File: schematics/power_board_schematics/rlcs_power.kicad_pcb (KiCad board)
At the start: 2 copper layers, 57.2 x 105.4 mm, 55 parts, among them J1 Conn_01x05_Male, J2 Conn_01x05_Male, J3 SD_Card, J4 Battery Conn, J5 Battery Conn, J6 CONN_01X02, J7 CONN_01X02, J8 CONN_01X02, Q1 Q_NPN_BEC, Q2 Q_NPN_BEC, T1 12 to 3v3, T2 12 to 5

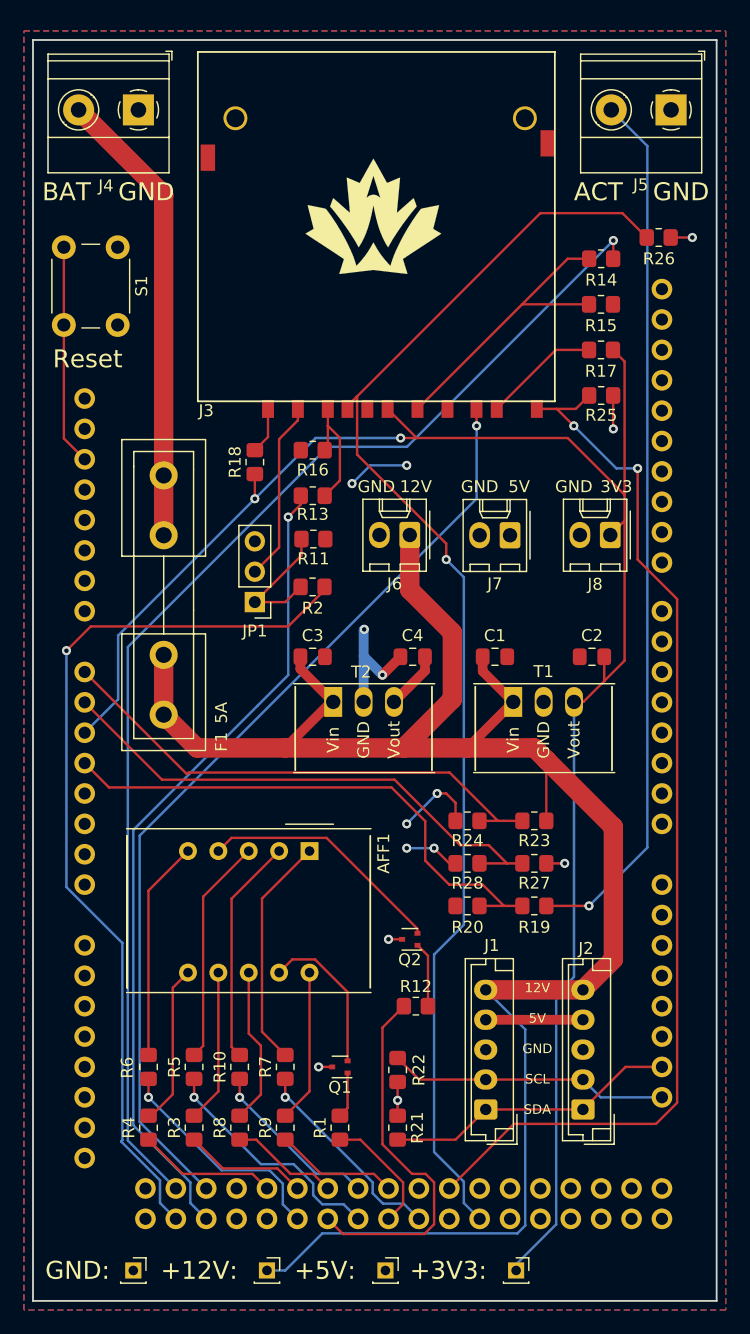
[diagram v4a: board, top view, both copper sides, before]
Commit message: Update Towerside Power Board PCB layout
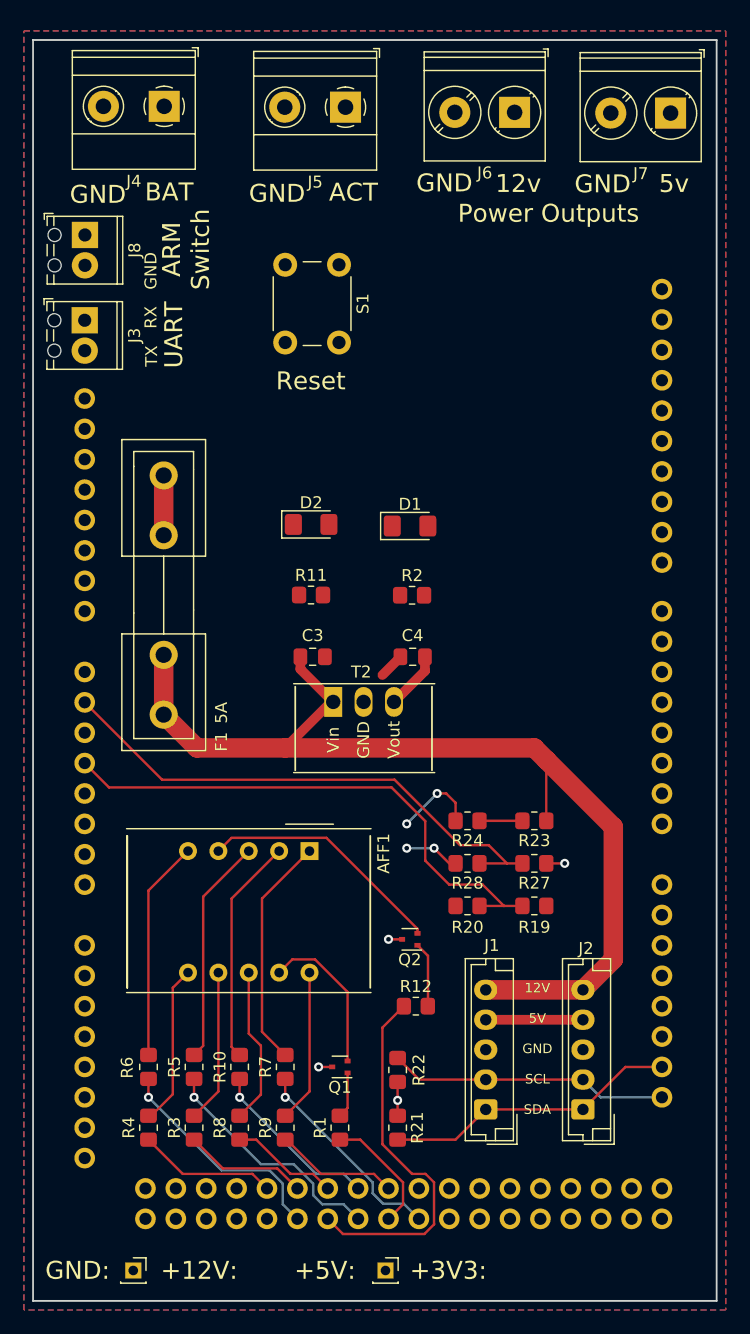
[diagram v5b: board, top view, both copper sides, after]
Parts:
- removed C1: 10uF, Capacitor_SMD:C_0805_2012Metric_Pad1.15x1.40mm_HandSolder
- removed C2: 22uF, Capacitor_SMD:C_0805_2012Metric_Pad1.15x1.40mm_HandSolder
- removed G*** (x2): LOGO, rlcs_power_footprints:rocketry_logo_small_noletters
- removed JP1: Jumper_NC_Dual, Connector_PinHeader_2.54mm:PinHeader_1x03_P2.54mm_Vertical
- removed R13, R14, R25, R26: 10K, Resistor_SMD:R_0805_2012Metric_Pad1.20x1.40mm_HandSolder
- removed R15, R16, R17, R18: 20K, Resistor_SMD:R_0805_2012Metric_Pad1.20x1.40mm_HandSolder
- removed T1: 12 to 3v3, rlcs_power_footprints:VXO78XX-1000
- removed TP1: 12v_test, Connector_PinSocket_2.00mm:PinSocket_1x01_P2.00mm_Vertical
- removed TP2: 3v3_test, Connector_PinSocket_2.00mm:PinSocket_1x01_P2.00mm_Vertical
- added D1: Green, LED_SMD:LED_1206_3216Metric_Pad1.42x1.75mm_HandSolder, F.Cu at (124.2, 102.9)
- added D2: Red, LED_SMD:LED_1206_3216Metric_Pad1.42x1.75mm_HandSolder, F.Cu at (116.0, 102.7)
- F1: value Fuse_Small -> 5A
- J3: value SD_Card -> UART Conn; footprint rlcs_power_footprints:SDCARD -> TerminalBlock_Phoenix:TerminalBlock_Phoenix_MPT-0,5-2-2.54_1x02_P2.54mm_Horizontal
- J4: value Battery Conn -> Power Board Power Input; footprint TerminalBlock_Phoenix:TerminalBlock_Phoenix_MKDS-1,5-2_1x02_P5.00mm_Horizontal -> TerminalBlock_Phoenix:TerminalBlock_Phoenix_MKDS-1,5-2-5.08_1x02_P5.08mm_Horizontal
- J5: value Battery Conn -> Actuator Battery Conn; footprint TerminalBlock_Phoenix:TerminalBlock_Phoenix_MKDS-1,5-2_1x02_P5.00mm_Horizontal -> TerminalBlock_Phoenix:TerminalBlock_Phoenix_MKDS-1,5-2-5.08_1x02_P5.08mm_Horizontal
- J6: value CONN_01X02 -> 12v Output; footprint Connector_Molex:Molex_KK-254_AE-6410-02A_1x02_P2.54mm_Vertical -> TerminalBlock_Phoenix:TerminalBlock_Phoenix_PT-1,5-2-5.0-H_1x02_P5.00mm_Horizontal
- J7: value CONN_01X02 -> 5v Output; footprint Connector_Molex:Molex_KK-254_AE-6410-02A_1x02_P2.54mm_Vertical -> TerminalBlock_Phoenix:TerminalBlock_Phoenix_PT-1,5-2-5.0-H_1x02_P5.00mm_Horizontal
- J8: value CONN_01X02 -> Keylock Switch Conn; footprint Connector_Molex:Molex_KK-254_AE-6410-02A_1x02_P2.54mm_Vertical -> TerminalBlock_Phoenix:TerminalBlock_Phoenix_MPT-0,5-2-2.54_1x02_P2.54mm_Horizontal
- R11: value 10K -> 150
- R2: value 20K -> 150
- moved J8 50.6 mm to (97.0, 78.5), turned to -90 degrees
- moved J7 37.8 mm to (146.0, 68.3)
- moved J6 36.4 mm to (133.0, 68.3)
- moved J5 27.2 mm to (118.8, 67.8)
- moved J3 25.8 mm to (97.0, 85.7), turned to -90 degrees
- moved S1 18.6 mm to (118.3, 81.0)
- moved R2 8.35 mm to (124.4, 108.7)
- moved R11 4.68 mm to (116.0, 108.6), turned to 0 degrees
- moved J4 2.18 mm to (103.7, 67.8)
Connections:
- J3 pad 1: Net-(J3-Pad1) -> ARD_UART_TX
- J3 pad 2: Net-(J3-Pad2) -> ARD_UART_RX
- J4 pad 1: GND -> Net-(F1-Pad1)
- J4 pad 2: Net-(F1-Pad1) -> GND
- J5 pad 1: GND -> /ACTUATOR_BAT
- J5 pad 2: /ACTUATOR_BAT -> GND
- J8 pad 1: SENSE_3V -> ARD_ARM_SWITCH
- R1 pad 1: Sevenseg_D2 -> Sevenseg_D1
- R11 pad 1: GND -> ARD_LED_ARMED
- R11 pad 2: Net-(JP1-Pad1) -> Net-(D2-Pad2)
- R12 pad 1: Sevenseg_D1 -> Sevenseg_D2
- R2 pad 1: Net-(JP1-Pad1) -> ARD_LED_CLIENT_COMM
- R2 pad 2: ARD_CON_SD_SS -> Net-(D1-Pad2)
- XA1 pad A0: SENSE_12V -> unconnected-(XA1-PadA0)
- XA1 pad A2: SENSE_3V -> unconnected-(XA1-PadA2)
- XA1 pad A4: unconnected-(XA1-PadA4) -> SENSE_12V
- XA1 pad D0: unconnected-(XA1-PadD0) -> ARD_UART_RX
- XA1 pad D1: unconnected-(XA1-PadD1) -> ARD_UART_TX
- XA1 pad D33: ARD_CON_SD_CD -> unconnected-(XA1-PadD33)
- XA1 pad D34: ARD_CON_SD_WP -> ARD_ARM_SWITCH
- XA1 pad D35: unconnected-(XA1-PadD35) -> ARD_LED_CLIENT_COMM
- XA1 pad D36: unconnected-(XA1-PadD36) -> ARD_LED_ARMED
- XA1 pad D39: Sevenseg_D2 -> Sevenseg_D1
- XA1 pad D43: Sevenseg_D1 -> Sevenseg_D2
- XA1 pad D50: ARD_CON_SD_MISO -> unconnected-(XA1-PadD50)
- XA1 pad D51: ARD_CON_SD_MOSI -> unconnected-(XA1-PadD51)
- XA1 pad D52: ARD_CON_SD_SCK -> unconnected-(XA1-PadD52)
- XA1 pad D53: ARD_CON_SD_SS -> unconnected-(XA1-PadD53)
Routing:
- net SENSE_3V: track 151.2 -> 0.00 mm, vias 2 -> 0
- net ARD_CON_SD_CD: track 107.8 -> 0.00 mm, vias 1 -> 0
- net ARD_CON_SD_SCK: track 103.1 -> 0.00 mm, vias 1 -> 0
- net ARD_CON_SD_WP: track 90.1 -> 0.00 mm, vias 2 -> 0
- net ARD_CON_SD_MISO: track 79.1 -> 0.00 mm, vias 1 -> 0
- net +12V: track 160.3 -> 84.9 mm
- net ARD_CON_SD_SS: track 75.3 -> 0.00 mm, vias 1 -> 0
- net /ACTUATOR_BAT: track 73.4 -> 0.00 mm, vias 1 -> 0
- net ARD_CON_SD_MOSI: track 68.8 -> 0.00 mm, vias 1 -> 0
- net SENSE_12V: track 43.4 -> 3.59 mm
- net Net-(F1-Pad1): track 38.5 -> 5.00 mm
- net Net-(J3-Pad5): track 25.1 -> 0.00 mm
- net Sevenseg_D2: track 10.3 -> 31.2 mm
- net Sevenseg_D1: track 31.2 -> 10.3 mm
- net Net-(S1-Pad2): track 18.4 -> 0.00 mm
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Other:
- board text added: "12v"
- board text added: "5v"
- board text added: "ARM Switch"
- board text added: "Power Outputs"
- board text added: "RX"
- board text added: "TX"
- board text added: "UART"

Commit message: Layout Towerside Power Board
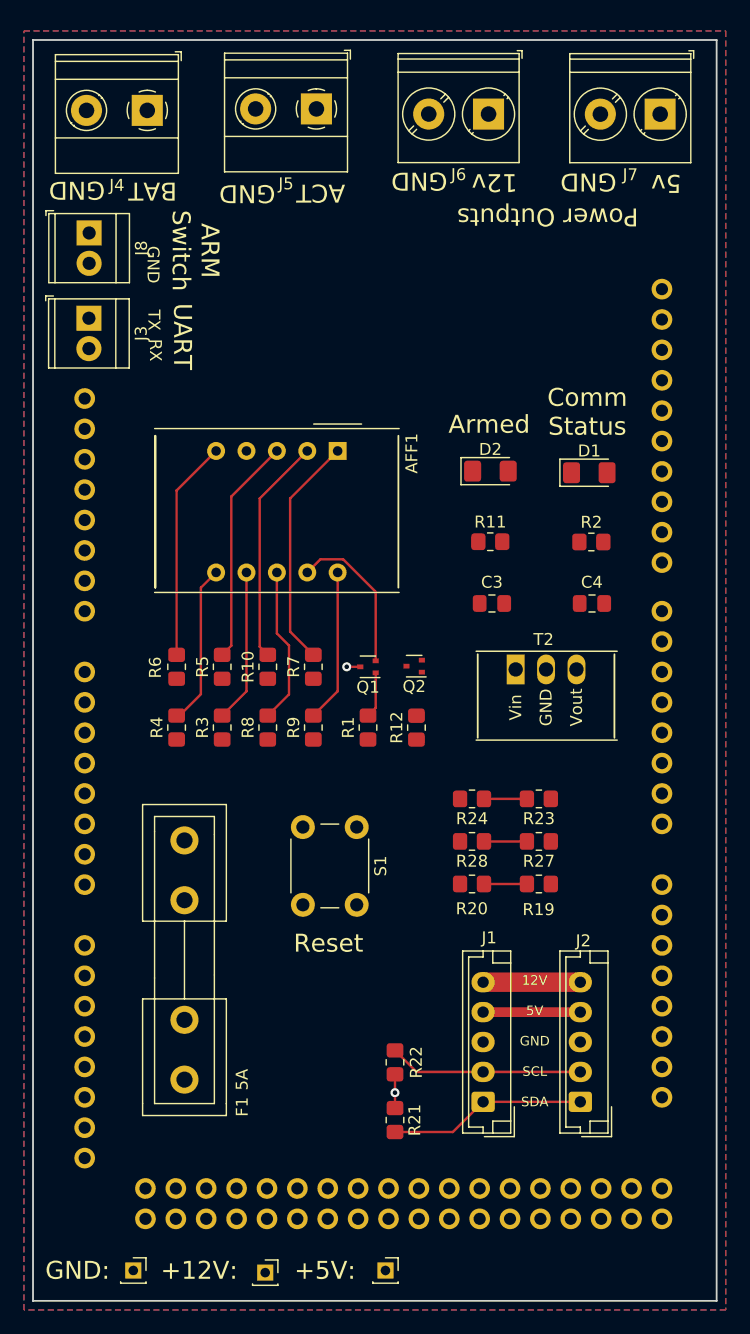
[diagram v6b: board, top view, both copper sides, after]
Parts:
- added TP1: 12v_test, Connector_PinSocket_2.00mm:PinSocket_1x01_P2.00mm_Vertical, F.Cu at (112.1, 165.3)
- J3, J8: footprint TerminalBlock_Phoenix:TerminalBlock_Phoenix_MPT-0,5-2-2.54_1x02_P2.54mm_Horizontal -> TerminalBlock_TE-Connectivity:TerminalBlock_TE_282834-2_1x02_P2.54mm_Horizontal
- moved S1 47.0 mm to (119.8, 128.0)
- moved R1 33.5 mm to (120.7, 119.7)
- moved R3 33.5 mm to (108.5, 119.7)
- moved R4 33.5 mm to (104.7, 119.7)
- moved R8 33.5 mm to (112.3, 119.7)
- moved R9 33.5 mm to (116.1, 119.7)
- moved AFF1 33.5 mm to (118.2, 96.6)
- moved Q1 33.5 mm to (120.7, 114.6)
- moved R10 33.5 mm to (112.3, 114.6)
- moved R5 33.5 mm to (108.5, 114.6)
- moved R6 33.5 mm to (104.7, 114.6)
- moved R7 33.5 mm to (116.1, 114.6)
- moved F1 30.6 mm to (105.4, 129.1)
- moved R12 23.3 mm to (124.8, 119.7), turned to 90 degrees
- moved Q2 22.8 mm to (124.6, 114.6)
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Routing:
- net +12V: track 84.9 -> 8.13 mm
- net SENSE_ACTUATOR: track 45.5 -> 3.59 mm
- net SENSE_5V: track 44.5 -> 3.59 mm
- net Sevenseg_D2: track 31.2 -> 0.00 mm
- net Net-(AFF1-Pad4): track 20.6 -> 0.00 mm
- net Sevenseg_E: track 20.0 -> 0.00 mm, vias 1 -> 0
- net Sevenseg_D: track 19.2 -> 0.00 mm, vias 1 -> 0
- net Sevenseg_C: track 17.5 -> 0.00 mm, vias 1 -> 0
- net Sevenseg_DP: track 14.6 -> 0.00 mm, vias 1 -> 0
- net GND: track 13.7 -> 0.00 mm, vias 4 -> 0
- net Sevenseg_F: track 11.6 -> 0.00 mm
- net Sevenseg_G: track 10.3 -> 0.00 mm
- net Sevenseg_A: track 10.3 -> 0.00 mm
- net Sevenseg_D1: track 10.3 -> 0.00 mm
- net Sevenseg_B: track 9.06 -> 0.00 mm
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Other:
- board text added: "Armed"
- board text added: "Comm Status"
- board text added: "RLCSv3 Power Board {dblquote}The Juice{dblquote} R4 2022-11-02 Jack Christensen Jason Xu"
- board text removed: "+3V3:"
- board text removed: "RLCSv3 Power Board {dblquote}The Juice{dblquote} R3 2022-01-27 Jack Christensen"

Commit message: Update Towerside Power Board silkscreen
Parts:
- moved S1 2.48 mm to (120.1, 130.5)
- moved TP4 2.02 mm to (124.2, 165.3)
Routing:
- net +12V: track 8.13 -> 0.00 mm
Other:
- board text added: "Current State"
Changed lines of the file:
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@@
       (effects (font (size 0.8 0.8) (thickness 0.15)))
     )
-    (fp_text user "GND" (at 5.08 4.318) (layer "F.SilkS")
+    (fp_text user "GND" (at 5.08 4.318 180) (layer "F.SilkS")
       (effects (font (size 0.8 0.8) (thickness 0.15)))
     )
-    (fp_text user "5V" (at 7.62 4.318) (layer "F.SilkS")
+    (fp_text user "5V" (at 7.62 4.318 180) (layer "F.SilkS")
       (effects (font (size 0.8 0.8) (thickness 0.15)))
     )
-    (fp_text user "SDA" (at 0 4.318) (layer "F.SilkS")
+    (fp_text user "SDA" (at 0 4.318 180) (layer "F.SilkS")
       (effects (font (size 0.8 0.8) (thickness 0.15)))
     )
@@
   )
   (footprint "Connector_PinSocket_2.00mm:PinSocket_1x01_P2.00mm_Vertical" (layer "F.Cu")
-    (at 122.174 165.1)
+    (at 124.19 165.28)
     (descr "Through hole straight socket strip, 1x01, 2.00mm pitch, single row (from Kicad 4.0.7), script generated")
     (tags "Through hole socket strip THT 1x01 2.00mm single row")
@@
   )
   (footprint "Button_Switch_THT:SW_PUSH_6mm" (layer "F.Cu")
-    (at 119.77 128.03 -90)
+    (at 120.08 130.49 -90)
     (descr "https://www.omron.com/ecb/products/pdf/en-b3f.pdf")
     (tags "tact sw push 6mm")
@@
     (effects (font (size 1.2 1.2) (thickness 0.15)) (justify left mirror))
   )
-  (gr_text "Armed" (at 130.85 94.37) (layer "F.SilkS")
+  (gr_text "Armed" (at 130.85 94.37 180) (layer "F.SilkS")
     (effects (font (size 1.5 1.5) (thickness 0.3)))
   )
-  (gr_text "RX" (at 102.95 88.16 -90) (layer "F.SilkS")
+  (gr_text "RX" (at 103.22 88.15 -90) (layer "F.SilkS")
     (effects (font (size 1 1) (thickness 0.15)))
   )
@@
     (effects (font (size 1.5 1.5) (thickness 0.3)) (justify left))
   )
-  (gr_text "TX" (at 102.82 85.65 -90) (layer "F.SilkS")
+  (gr_text "TX" (at 103.26 85.6 -90) (layer "F.SilkS")
     (effects (font (size 1 1) (thickness 0.15)))
   )
@@
     (effects (font (size 1.5 1.5) (thickness 0.3)) (justify left))
   )
-  (gr_text "UART" (at 105.2 87.02 -90) (layer "F.SilkS")
+  (gr_text "Current State" (at 113.09 92.56 180) (layer "F.SilkS")
+    (effects (font (size 1.5 1.5) (thickness 0.3)))
+  )
+  (gr_text "UART" (at 105.39 87.27 -90) (layer "F.SilkS")
     (effects (font (size 1.5 1.5) (thickness 0.3)))
   )
@@
     (effects (font (size 1.5 1.5) (thickness 0.3)) (justify left))
   )
-  (gr_text "+5V:" (at 114.554 165.1) (layer "F.SilkS")
+  (gr_text "+5V:" (at 131.36 165.28 180) (layer "F.SilkS")
     (effects (font (size 1.5 1.5) (thickness 0.3)) (justify left))
   )
-  (gr_text "GND" (at 102.75 81.01 -90) (layer "F.SilkS")
+  (gr_text "GND" (at 103.37 80.96 -90) (layer "F.SilkS")
     (effects (font (size 1 1) (thickness 0.15)))
   )
-  (gr_text "+12V:" (at 103.378 165.1) (layer "F.SilkS")
+  (gr_text "+12V:" (at 120.75 165.3 180) (layer "F.SilkS")
     (effects (font (size 1.5 1.5) (thickness 0.3)) (justify left))
   )
-  (gr_text "GND:\n" (at 93.726 165.1) (layer "F.SilkS")
+  (gr_text "GND:\n" (at 108.16 165.2 180) (layer "F.SilkS")
     (effects (font (size 1.5 1.5) (thickness 0.3)) (justify left))
   )
-  (gr_text "ARM\nSwitch" (at 106.29 79.84 -90) (layer "F.SilkS")
+  (gr_text "ARM\nSwitch" (at 106.75 79.85 -90) (layer "F.SilkS")
     (effects (font (size 1.5 1.5) (thickness 0.3)))
   )
@@
     (effects (font (size 1.5 1.5) (thickness 0.3)) (justify left))
   )
-  (gr_text "12v" (at 133.22 74.14 180) (layer "F.SilkS")
+  (gr_text "12v" (at 133.33 74.08 180) (layer "F.SilkS")
     (effects (font (size 1.5 1.5) (thickness 0.3)) (justify left))
   )
-  (gr_text "Comm\nStatus" (at 139.05 93.33) (layer "F.SilkS")
+  (gr_text "Comm\nStatus" (at 139.05 93.33 180) (layer "F.SilkS")
     (effects (font (size 1.5 1.5) (thickness 0.3)))
   )
-  (gr_text "Reset" (at 117.41 137.75) (layer "F.SilkS")
+  (gr_text "Reset" (at 117.78 127.51 180) (layer "F.SilkS")
     (effects (font (size 1.5 1.5) (thickness 0.3)))
   )
@@
   (segment (start 116.74 105.64) (end 118.632642 105.64) (width 0.2032) (layer "F.Cu") (net 22))
   (segment (start 115.634889 106.745111) (end 116.74 105.64) (width 0.2032) (layer "F.Cu") (net 22))
-  (segment (start 138.464 141) (end 130.336 141) (width 1.6256) (layer "F.Cu") (net 26))
   (segment (start 130.41 125.674) (end 133.998 125.674) (width 0.2032) (layer "F.Cu") (net 38))
   (segment (start 130.41 129.23) (end 133.998 129.23) (width 0.2032) (layer "F.Cu") (net 39))

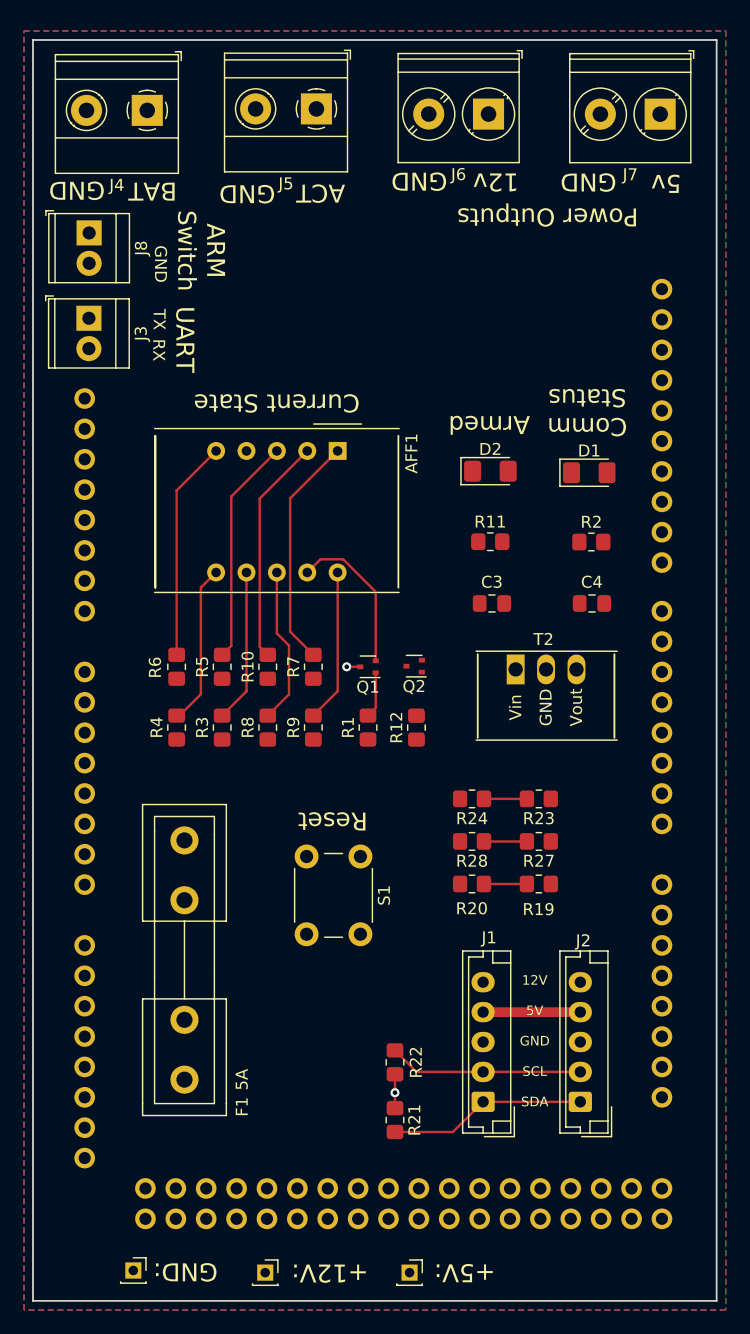
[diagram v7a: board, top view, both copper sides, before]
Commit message: Route Towerside Power Board
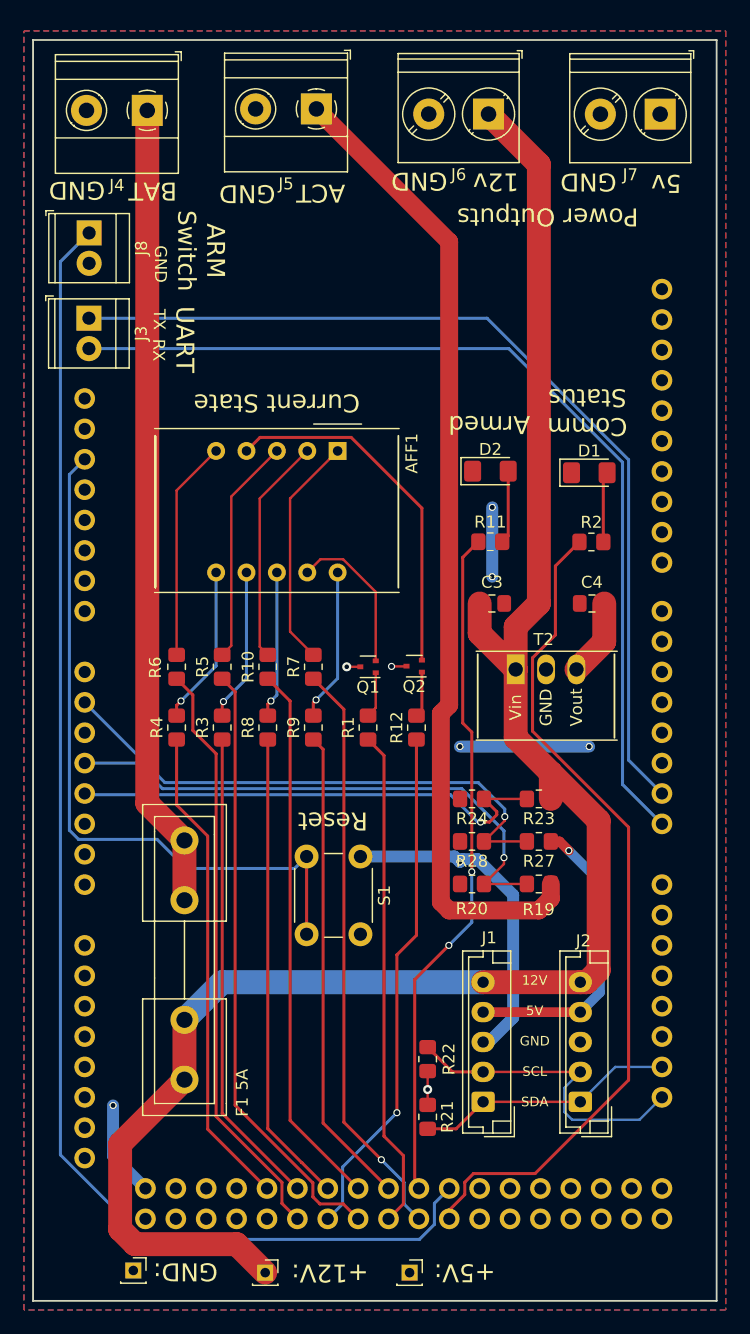
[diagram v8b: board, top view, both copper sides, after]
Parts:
- moved R21 2.74 mm to (125.7, 152.3)
- moved R22 2.74 mm to (125.7, 147.4)
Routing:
- net +12V: track 0.00 -> 155.7 mm
- net ARD_ARM_SWITCH: track 0.00 -> 116.3 mm
- net /ACTUATOR_BAT: track 0.00 -> 82.3 mm
- net ARD_UART_RX: track 0.00 -> 80.1 mm
- net ARD_UART_TX: track 0.00 -> 79.1 mm
- net ARD_LED_CLIENT_COMM: track 0.00 -> 70.8 mm
- net Net-(F1-Pad1): track 0.00 -> 67.3 mm
- net Net-(S1-Pad2): track 0.00 -> 59.6 mm
- net ARD_LED_ARMED: track 0.00 -> 57.0 mm, vias 0 -> 2
- net GND: track 0.00 -> 52.6 mm, vias 0 -> 6
- net Sevenseg_E: track 0.00 -> 51.0 mm
- net Sevenseg_D: track 0.00 -> 49.3 mm
- net Sevenseg_C: track 0.00 -> 48.8 mm, vias 0 -> 1
- net Sevenseg_DP: track 0.00 -> 45.7 mm
- net Sevenseg_D2: track 0.00 -> 43.1 mm, vias 0 -> 1
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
